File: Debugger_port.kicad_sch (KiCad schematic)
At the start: 5 parts, among them J10 Conn_01x06_Female

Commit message: v2.1 finished
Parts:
- removed D75, D76, D77, D78: SM6T33A, _Diodes:SM2T3V3A, symbol Diode:SM6T33A
- added D75, D76, D77, D78, D97: AOZ8211, _Diodes:AOZ8211, symbol _Diodes:AOZ8211
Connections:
- net +3V3: now also D97.2
- net GND: now also D75.1, D76.1, D77.1, D78.1, D97.1
- net NRST: now also D78.2
- net SWCLK: now also D76.2
- net SWDIO: now also D75.2
- net SWO: now also D77.2
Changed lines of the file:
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@@
   (junction (at 151.13 118.11) (diameter 0) (color 0 0 0 0)
   )
+  (junction (at 182.88 88.9) (diameter 0) (color 0 0 0 0)
+  )
   (junction (at 151.13 96.52) (diameter 0) (color 0 0 0 0)
   )
@@
   (junction (at 153.1498 118.11) (diameter 0) (color 0 0 0 0)
   )
+  (wire (pts (xy 182.88 88.9) (xy 143.51 88.9))
+    (stroke (width 0) (type default) (color 0 0 0 0))
+  )
   (wire (pts (xy 151.13 118.11) (xy 153.1498 118.11))
     (stroke (width 0) (type default) (color 0 0 0 0))
@@
     (stroke (width 0) (type default) (color 0 0 0 0))
   )
+  (wire (pts (xy 191.77 88.9) (xy 182.88 88.9))
+    (stroke (width 0) (type default) (color 0 0 0 0))
+  )
   (wire (pts (xy 143.51 93.98) (xy 147.32 93.98))
     (stroke (width 0) (type default) (color 0 0 0 0))
@@
     (stroke (width 0) (type default) (color 0 0 0 0))
   )
+  (wire (pts (xy 182.88 114.3) (xy 182.88 121.92))
+    (stroke (width 0) (type default) (color 0 0 0 0))
+  )
   (wire (pts (xy 154.94 99.06) (xy 154.94 106.68))
     (stroke (width 0) (type default) (color 0 0 0 0))
@@
     (stroke (width 0) (type default) (color 0 0 0 0))
   )
+  (wire (pts (xy 182.88 88.9) (xy 182.88 106.68))
+    (stroke (width 0) (type default) (color 0 0 0 0))
+  )
   (wire (pts (xy 151.13 114.3) (xy 151.13 118.11))
     (stroke (width 0) (type default) (color 0 0 0 0))
@@
     (effects (font (size 1.27 1.27)) (justify left))
   )
-  (symbol (lib_id "Diode:SM6T33A") (at 151.13 110.49 270) (unit 1)
-    (in_bom yes) (on_board yes)
-    (property "Reference" "D76" (id 0) (at 148.59 107.95 90)
+  (symbol (lib_id "_Diodes:AOZ8211") (at 156.21 110.49 90) (unit 1)
+    (in_bom yes) (on_board yes)
+    (property "Reference" "D78" (id 0) (at 143.51 109.22 0)
+      (effects (font (size 1.27 1.27)) (justify right))
+    )
+    (property "Value" "AOZ8211" (id 1) (at 161.29 111.7599 90)
+      (effects (font (size 1.27 1.27)) (justify right) hide)
+    )
+    (property "Footprint" "_Diodes:AOZ8211" (id 2) (at 156.21 110.49 0)
+      (effects (font (size 1.27 1.27)) hide)
+    )
+    (property "Datasheet" "" (id 3) (at 156.21 110.49 0)
+      (effects (font (size 1.27 1.27)) hide)
+    )
+    (pin "1")
+    (pin "2")
+  )
+  (symbol (lib_id "_Diodes:AOZ8211") (at 152.4 110.49 90) (unit 1)
+    (in_bom yes) (on_board yes)
+    (property "Reference" "D77" (id 0) (at 140.97 109.22 0)
+      (effects (font (size 1.27 1.27)) (justify right))
+    )
+    (property "Value" "AOZ8211" (id 1) (at 157.48 111.7599 90)
+      (effects (font (size 1.27 1.27)) (justify right) hide)
+    )
+    (property "Footprint" "_Diodes:AOZ8211" (id 2) (at 152.4 110.49 0)
+      (effects (font (size 1.27 1.27)) hide)
+    )
+    (property "Datasheet" "" (id 3) (at 152.4 110.49 0)
+      (effects (font (size 1.27 1.27)) hide)
+    )
+    (pin "1")
+    (pin "2")
+  )
+  (symbol (lib_id "_Diodes:AOZ8211") (at 148.59 110.49 90) (unit 1)
+    (in_bom yes) (on_board yes)
+    (property "Reference" "D76" (id 0) (at 138.43 109.22 0)
+      (effects (font (size 1.27 1.27)) (justify right))
+    )
+    (property "Value" "AOZ8211" (id 1) (at 153.67 111.7599 90)
+      (effects (font (size 1.27 1.27)) (justify right) hide)
+    )
+    (property "Footprint" "_Diodes:AOZ8211" (id 2) (at 148.59 110.49 0)
+      (effects (font (size 1.27 1.27)) hide)
+    )
+    (property "Datasheet" "" (id 3) (at 148.59 110.49 0)
+      (effects (font (size 1.27 1.27)) hide)
+    )
+    (pin "1")
+    (pin "2")
+  )
+  (symbol (lib_id "power:+3.3V") (at 191.77 88.9 270) (unit 1)
+    (in_bom yes) (on_board yes) (fields_autoplaced)
+    (property "Reference" "#PWR0139" (id 0) (at 187.96 88.9 0)
+      (effects (font (size 1.27 1.27)) hide)
+    )
+    (property "Value" "+3.3V" (id 1) (at 195.58 88.8999 90)
       (effects (font (size 1.27 1.27)) (justify left))
     )
-    (property "Value" "SM6T33A" (id 1) (at 135.89 107.95 90)
-      (effects (font (size 1.27 1.27)) (justify left) hide)
-    )
-    (property "Footprint" "_Diodes:SM2T3V3A" (id 2) (at 146.05 110.49 0)
-      (effects (font (size 1.27 1.27)) hide)
-    )
-    (property "Datasheet" "https://www.st.com/resource/en/datasheet/sm6t.pdf" (id 3) (at 151.13 109.22 0)
-      (effects (font (size 1.27 1.27)) hide)
-    )
-    (pin "1")
-    (pin "2")
-  )
-  (symbol (lib_id "Diode:SM6T33A") (at 154.94 110.49 270) (unit 1)
-    (in_bom yes) (on_board yes)
-    (property "Reference" "D77" (id 0) (at 152.4 107.95 90)
-      (effects (font (size 1.27 1.27)) (justify left))
-    )
-    (property "Value" "SM6T33A" (id 1) (at 135.89 110.49 90)
-      (effects (font (size 1.27 1.27)) (justify left) hide)
-    )
-    (property "Footprint" "_Diodes:SM2T3V3A" (id 2) (at 149.86 110.49 0)
-      (effects (font (size 1.27 1.27)) hide)
-    )
-    (property "Datasheet" "https://www.st.com/resource/en/datasheet/sm6t.pdf" (id 3) (at 154.94 109.22 0)
-      (effects (font (size 1.27 1.27)) hide)
-    )
-    (pin "1")
-    (pin "2")
-  )
-  (symbol (lib_id "power:+3.3V") (at 143.51 88.9 270) (unit 1)
-    (in_bom yes) (on_board yes) (fields_autoplaced)
-    (property "Reference" "#PWR0139" (id 0) (at 139.7 88.9 0)
-      (effects (font (size 1.27 1.27)) hide)
-    )
-    (property "Value" "+3.3V" (id 1) (at 147.32 88.8999 90)
-      (effects (font (size 1.27 1.27)) (justify left))
-    )
-    (property "Footprint" "" (id 2) (at 143.51 88.9 0)
-      (effects (font (size 1.27 1.27)) hide)
-    )
-    (property "Datasheet" "" (id 3) (at 143.51 88.9 0)
+    (property "Footprint" "" (id 2) (at 191.77 88.9 0)
+      (effects (font (size 1.27 1.27)) hide)
+    )
+    (property "Datasheet" "" (id 3) (at 191.77 88.9 0)
       (effects (font (size 1.27 1.27)) hide)
     )
@@
     (pin "6")
   )
-  (symbol (lib_id "Diode:SM6T33A") (at 158.75 110.49 270) (unit 1)
-    (in_bom yes) (on_board yes)
-    (property "Reference" "D78" (id 0) (at 156.21 107.95 90)
-      (effects (font (size 1.27 1.27)) (justify left))
-    )
-    (property "Value" "SM6T33A" (id 1) (at 135.89 113.03 90)
-      (effects (font (size 1.27 1.27)) (justify left) hide)
-    )
-    (property "Footprint" "_Diodes:SM2T3V3A" (id 2) (at 153.67 110.49 0)
-      (effects (font (size 1.27 1.27)) hide)
-    )
-    (property "Datasheet" "https://www.st.com/resource/en/datasheet/sm6t.pdf" (id 3) (at 158.75 109.22 0)
+  (symbol (lib_id "_Diodes:AOZ8211") (at 144.78 110.49 90) (unit 1)
+    (in_bom yes) (on_board yes)
+    (property "Reference" "D75" (id 0) (at 135.89 109.22 0)
+      (effects (font (size 1.27 1.27)) (justify right))
+    )
+    (property "Value" "AOZ8211" (id 1) (at 135.89 114.3 90)
+      (effects (font (size 1.27 1.27)) (justify right))
+    )
+    (property "Footprint" "_Diodes:AOZ8211" (id 2) (at 144.78 110.49 0)
+      (effects (font (size 1.27 1.27)) hide)
+    )
+    (property "Datasheet" "" (id 3) (at 144.78 110.49 0)
       (effects (font (size 1.27 1.27)) hide)
     )
@@
     (pin "1")
   )
-  (symbol (lib_id "Diode:SM6T33A") (at 147.32 110.49 270) (unit 1)
-    (in_bom yes) (on_board yes)
-    (property "Reference" "D75" (id 0) (at 144.78 107.95 90)
-      (effects (font (size 1.27 1.27)) (justify left))
-    )
-    (property "Value" "SM6T33A" (id 1) (at 135.89 110.49 90)
-      (effects (font (size 1.27 1.27)) (justify left))
-    )
-    (property "Footprint" "_Diodes:SM2T3V3A" (id 2) (at 142.24 110.49 0)
-      (effects (font (size 1.27 1.27)) hide)
-    )
-    (property "Datasheet" "https://www.st.com/resource/en/datasheet/sm6t.pdf" (id 3) (at 147.32 109.22 0)
-      (effects (font (size 1.27 1.27)) hide)
-    )
+  (symbol (lib_id "power:GND") (at 182.88 121.92 0) (unit 1)
+    (in_bom yes) (on_board yes) (fields_autoplaced)
+    (property "Reference" "#PWR0207" (id 0) (at 182.88 128.27 0)
+      (effects (font (size 1.27 1.27)) hide)
+    )
+    (property "Value" "GND" (id 1) (at 182.88 127 0))
+    (property "Footprint" "" (id 2) (at 182.88 121.92 0)
+      (effects (font (size 1.27 1.27)) hide)
+    )
+    (property "Datasheet" "" (id 3) (at 182.88 121.92 0)
+      (effects (font (size 1.27 1.27)) hide)
+    )
+    (pin "1")
+  )
+  (symbol (lib_id "_Diodes:AOZ8211") (at 180.34 110.49 90) (unit 1)
+    (in_bom yes) (on_board yes) (fields_autoplaced)
+    (property "Reference" "D97" (id 0) (at 185.42 109.2199 90)
+      (effects (font (size 1.27 1.27)) (justify right))
+    )
+    (property "Value" "AOZ8211" (id 1) (at 185.42 111.7599 90)
+      (effects (font (size 1.27 1.27)) (justify right))
+    )
+    (property "Footprint" "_Diodes:AOZ8211" (id 2) (at 180.34 110.49 0)
+      (effects (font (size 1.27 1.27)) hide)
+    )
+    (property "Datasheet" "" (id 3) (at 180.34 110.49 0)
+      (effects (font (size 1.27 1.27)) hide)
+    )

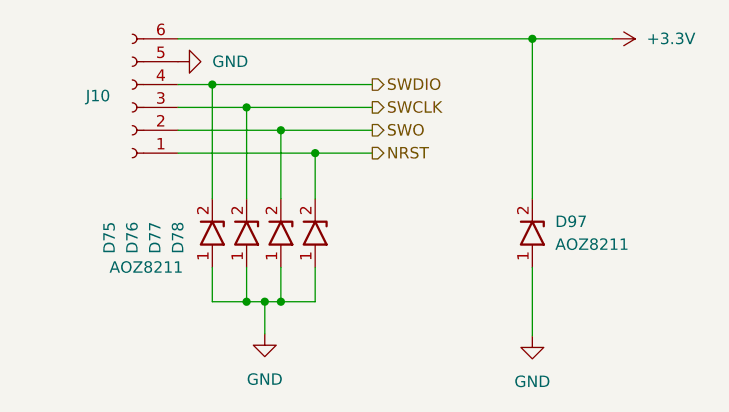
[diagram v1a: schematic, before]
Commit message: changed power loss detection schematic, changed tvs diodes on other type, added two more caps on 3v3 line, change indicator leds resistors
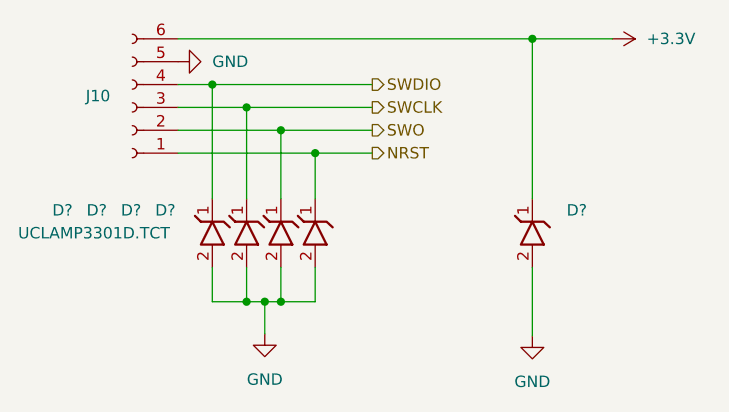
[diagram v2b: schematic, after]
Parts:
- removed D75, D76, D77, D78, D97: AOZ8211, _Diodes:AOZ8211, symbol _Diodes:AOZ8211
- added D? (x5): UCLAMP3301D.TCT, _Diodes:UCLAMP3301D.TCT, symbol _Diodes:UCLAMP3301D.TCT
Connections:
- net +3V3: now also D?.1
- net GND: now also D?.2, D?.2, D?.2, D?.2, D?.2
- net NRST: now also D?.1
- net SWCLK: now also D?.1
- net SWDIO: now also D?.1
- net SWO: now also D?.1
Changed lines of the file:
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@@
     (effects (font (size 1.27 1.27)) (justify left))
   )
-  (symbol (lib_id "_Diodes:AOZ8211") (at 156.21 110.49 90) (unit 1)
+  (symbol (lib_id "_Diodes:UCLAMP3301D.TCT") (at 154.94 118.11 0) (unit 1)
     (in_bom yes) (on_board yes)
-    (property "Reference" "D78" (id 0) (at 143.51 109.22 0)
-      (effects (font (size 1.27 1.27)) (justify right))
+    (property "Reference" "D?" (id 0) (at 137.16 107.95 0)
+      (effects (font (size 1.27 1.27)) (justify left))
     )
-    (property "Value" "AOZ8211" (id 1) (at 161.29 111.7599 90)
-      (effects (font (size 1.27 1.27)) (justify right) hide)
+    (property "Value" "UCLAMP3301D.TCT" (id 1) (at 139.7 127 90)
+      (effects (font (size 1.27 1.27)) (justify left) hide)
     )
-    (property "Footprint" "_Diodes:AOZ8211" (id 2) (at 156.21 110.49 0)
+    (property "Footprint" "_Diodes:UCLAMP3301D.TCT" (id 2) (at 154.94 118.11 0)
       (effects (font (size 1.27 1.27)) hide)
     )
-    (property "Datasheet" "" (id 3) (at 156.21 110.49 0)
+    (property "Datasheet" "" (id 3) (at 154.94 118.11 0)
       (effects (font (size 1.27 1.27)) hide)
     )
@@
     (pin "2")
   )
-  (symbol (lib_id "_Diodes:AOZ8211") (at 152.4 110.49 90) (unit 1)
+  (symbol (lib_id "_Diodes:UCLAMP3301D.TCT") (at 182.88 118.11 0) (unit 1)
     (in_bom yes) (on_board yes)
-    (property "Reference" "D77" (id 0) (at 140.97 109.22 0)
-      (effects (font (size 1.27 1.27)) (justify right))
+    (property "Reference" "D?" (id 0) (at 186.69 107.95 0)
+      (effects (font (size 1.27 1.27)) (justify left))
     )
-    (property "Value" "AOZ8211" (id 1) (at 157.48 111.7599 90)
-      (effects (font (size 1.27 1.27)) (justify right) hide)
+    (property "Value" "UCLAMP3301D.TCT" (id 1) (at 166.37 127 90)
+      (effects (font (size 1.27 1.27)) (justify left) hide)
     )
-    (property "Footprint" "_Diodes:AOZ8211" (id 2) (at 152.4 110.49 0)
+    (property "Footprint" "_Diodes:UCLAMP3301D.TCT" (id 2) (at 182.88 118.11 0)
       (effects (font (size 1.27 1.27)) hide)
     )
-    (property "Datasheet" "" (id 3) (at 152.4 110.49 0)
-      (effects (font (size 1.27 1.27)) hide)
-    )
-    (pin "1")
-    (pin "2")
-  )
-  (symbol (lib_id "_Diodes:AOZ8211") (at 148.59 110.49 90) (unit 1)
-    (in_bom yes) (on_board yes)
-    (property "Reference" "D76" (id 0) (at 138.43 109.22 0)
-      (effects (font (size 1.27 1.27)) (justify right))
-    )
-    (property "Value" "AOZ8211" (id 1) (at 153.67 111.7599 90)
-      (effects (font (size 1.27 1.27)) (justify right) hide)
-    )
-    (property "Footprint" "_Diodes:AOZ8211" (id 2) (at 148.59 110.49 0)
-      (effects (font (size 1.27 1.27)) hide)
-    )
-    (property "Datasheet" "" (id 3) (at 148.59 110.49 0)
+    (property "Datasheet" "" (id 3) (at 182.88 118.11 0)
       (effects (font (size 1.27 1.27)) hide)
     )
@@
     (pin "6")
   )
-  (symbol (lib_id "_Diodes:AOZ8211") (at 144.78 110.49 90) (unit 1)
+  (symbol (lib_id "_Diodes:UCLAMP3301D.TCT") (at 158.75 118.11 0) (unit 1)
     (in_bom yes) (on_board yes)
-    (property "Reference" "D75" (id 0) (at 135.89 109.22 0)
-      (effects (font (size 1.27 1.27)) (justify right))
+    (property "Reference" "D?" (id 0) (at 140.97 107.95 0)
+      (effects (font (size 1.27 1.27)) (justify left))
     )
-    (property "Value" "AOZ8211" (id 1) (at 135.89 114.3 90)
-      (effects (font (size 1.27 1.27)) (justify right))
+    (property "Value" "UCLAMP3301D.TCT" (id 1) (at 142.24 127 90)
+      (effects (font (size 1.27 1.27)) (justify left) hide)
     )
-    (property "Footprint" "_Diodes:AOZ8211" (id 2) (at 144.78 110.49 0)
+    (property "Footprint" "_Diodes:UCLAMP3301D.TCT" (id 2) (at 158.75 118.11 0)
       (effects (font (size 1.27 1.27)) hide)
     )
-    (property "Datasheet" "" (id 3) (at 144.78 110.49 0)
+    (property "Datasheet" "" (id 3) (at 158.75 118.11 0)
       (effects (font (size 1.27 1.27)) hide)
     )
@@
     )
     (pin "1")
+  )
+  (symbol (lib_id "_Diodes:UCLAMP3301D.TCT") (at 151.13 118.11 0) (unit 1)
+    (in_bom yes) (on_board yes)
+    (property "Reference" "D?" (id 0) (at 133.35 107.95 0)
+      (effects (font (size 1.27 1.27)) (justify left))
+    )
+    (property "Value" "UCLAMP3301D.TCT" (id 1) (at 137.16 127 90)
+      (effects (font (size 1.27 1.27)) (justify left) hide)
+    )
+    (property "Footprint" "_Diodes:UCLAMP3301D.TCT" (id 2) (at 151.13 118.11 0)
+      (effects (font (size 1.27 1.27)) hide)
+    )
+    (property "Datasheet" "" (id 3) (at 151.13 118.11 0)
+      (effects (font (size 1.27 1.27)) hide)
+    )
+    (pin "1")
+    (pin "2")
   )
   (symbol (lib_id "power:GND") (at 153.1498 121.6738 0) (unit 1)
@@
     (pin "1")
   )
-  (symbol (lib_id "_Diodes:AOZ8211") (at 180.34 110.49 90) (unit 1)
-    (in_bom yes) (on_board yes) (fields_autoplaced)
-    (property "Reference" "D97" (id 0) (at 185.42 109.2199 90)
-      (effects (font (size 1.27 1.27)) (justify right))
+  (symbol (lib_id "_Diodes:UCLAMP3301D.TCT") (at 147.32 118.11 0) (unit 1)
+    (in_bom yes) (on_board yes)
+    (property "Reference" "D?" (id 0) (at 129.54 107.95 0)
+      (effects (font (size 1.27 1.27)) (justify left))
     )
-    (property "Value" "AOZ8211" (id 1) (at 185.42 111.7599 90)
-      (effects (font (size 1.27 1.27)) (justify right))
+    (property "Value" "UCLAMP3301D.TCT" (id 1) (at 125.73 110.49 0)
+      (effects (font (size 1.27 1.27)) (justify left))
     )
-    (property "Footprint" "_Diodes:AOZ8211" (id 2) (at 180.34 110.49 0)
+    (property "Footprint" "_Diodes:UCLAMP3301D.TCT" (id 2) (at 147.32 118.11 0)
       (effects (font (size 1.27 1.27)) hide)
     )
-    (property "Datasheet" "" (id 3) (at 180.34 110.49 0)
+    (property "Datasheet" "" (id 3) (at 147.32 118.11 0)
       (effects (font (size 1.27 1.27)) hide)
     )
